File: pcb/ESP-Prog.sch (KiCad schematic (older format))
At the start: 27 parts, among them J1 UJ2-MIBH-G-SMT-TR, J2 Conn_01x03, J3 Conn_02x05_Odd_Even, J4 Conn_01x03, J5 Conn_01x03, J6 Conn_02x03_Odd_Even, Q1 MMSS8050-H-TP, Q2 MMSS8050-H-TP, U1 LD1117S33TR_SOT223

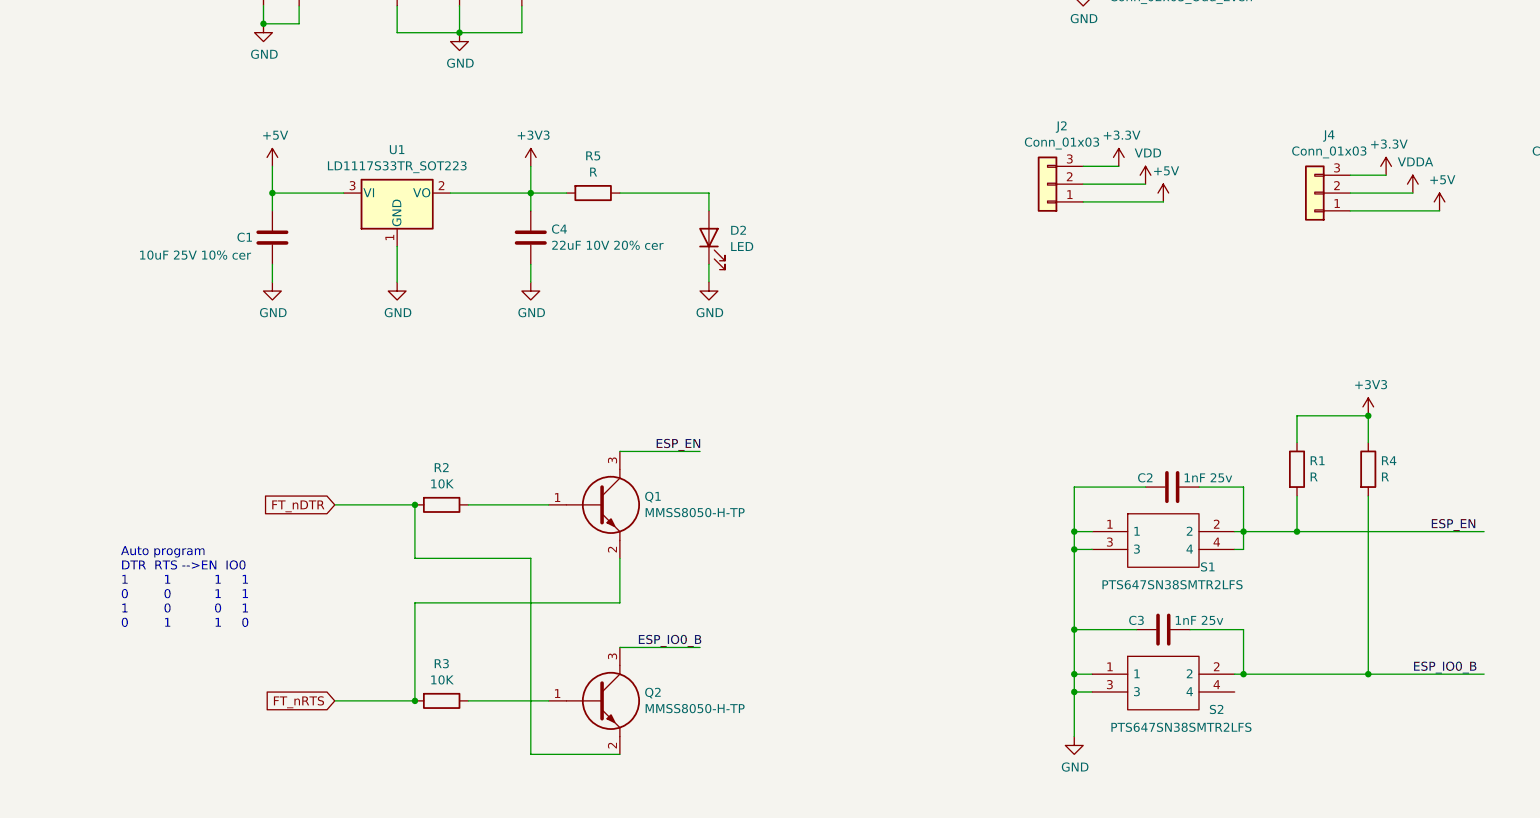
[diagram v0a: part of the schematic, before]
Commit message: correcciones al esquematico y avances en posicionamiento de pcb
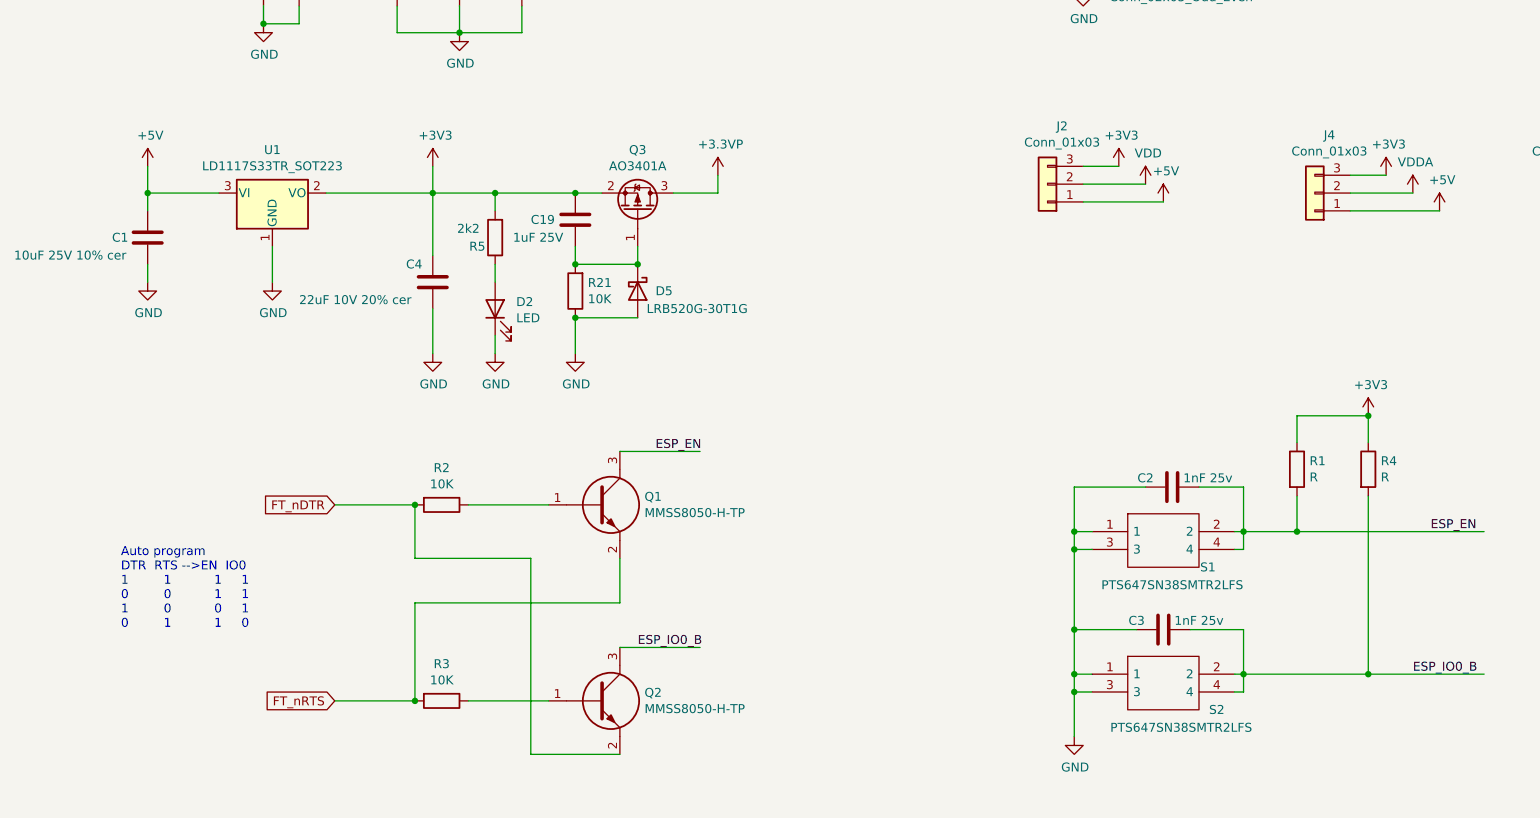
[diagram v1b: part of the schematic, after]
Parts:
- added C19: 1uF 25V, Capacitor_SMD:C_0603_1608Metric, symbol Device:C
- added D5: LRB520G-30T1G, Diode_SMD:D_0603_1608Metric, symbol Device:D_Schottky
- added Q3: AO3401A, Package_TO_SOT_SMD:SOT-23, symbol Transistor_FET:AO3401A
- added R21: 10K, Resistor_SMD:R_0603_1608Metric, symbol Device:R
- R5: value R -> 2k2
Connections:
- net labels added: +3.3VP
- net labels removed: +3.3V
- wire segments 106 -> 117
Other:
- moved on the sheet: C1, C4, D2, R5, U1

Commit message: - Se modifica el esquemático para respetar la estructura gerarquica
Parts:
- removed C1: 10uF 25V 10% cer, Capacitor_SMD:C_0603_1608Metric, symbol Device:C
- removed C19: 1uF 25V, Capacitor_SMD:C_0603_1608Metric, symbol Device:C
- removed C2, C3: 1nF 25v, Capacitor_SMD:C_0603_1608Metric, symbol Device:C
- removed C4: 22uF 10V 20% cer, Capacitor_SMD:C_0603_1608Metric, symbol Device:C
- removed C7, C8: 0.1uF 25v, Capacitor_SMD:C_0603_1608Metric, symbol Device:C
- removed D1: BAT760-7, Diode_SMD:D_SOD-323, symbol SamacSys_Parts:BAT760-7
- removed D2: LED, LED_SMD:LED_0603_1608Metric, symbol Device:LED
- removed D5: LRB520G-30T1G, Diode_SMD:D_0603_1608Metric, symbol Device:D_Schottky
- removed D7, D8, D9: D_TVS, Diode_SMD:D_SOD-523, symbol Device:D_TVS
- removed J1: UJ2-MIBH-G-SMT-TR, SamacSys_Parts:UJ2MIBHGSMTTR, symbol SamacSys_Parts:UJ2-MIBH-G-SMT-TR
- removed J2, J4, J5: Conn_01x03, Connector_PinHeader_2.54mm:PinHeader_1x03_P2.54mm_Vertical, symbol Connector_Generic:Conn_01x03
- removed J3: Conn_02x05_Odd_Even, Connector_PinHeader_1.27mm:PinHeader_2x05_P1.27mm_Vertical_SMD, symbol Connector_Generic:Conn_02x05_Odd_Even
- removed J6: Conn_02x03_Odd_Even, Connector_PinHeader_1.27mm:PinHeader_2x05_P1.27mm_Vertical_SMD, symbol Connector_Generic:Conn_02x03_Odd_Even
- removed Q1, Q2: MMSS8050-H-TP, SamacSys_Parts:SI2305TP, symbol SamacSys_Parts:MMSS8050-H-TP
- removed Q3: AO3401A, Package_TO_SOT_SMD:SOT-23, symbol Transistor_FET:AO3401A
- removed R1, R4: R, Resistor_SMD:R_0603_1608Metric, symbol Device:R
- removed R2, R21, R3: 10K, Resistor_SMD:R_0603_1608Metric, symbol Device:R
- removed R5: 2k2, Resistor_SMD:R_0603_1608Metric, symbol Device:R
- removed S1, S2: PTS647SN38SMTR2LFS, SamacSys_Parts:PTS647SM38SMTR2LFS, symbol SamacSys_Parts:PTS647SN38SMTR2LFS
- removed U1: LD1117S33TR_SOT223, Package_TO_SOT_SMD:SOT-223-3_TabPin2, symbol Regulator_Linear:LD1117S33TR_SOT223
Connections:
- net labels removed: +3.3VP, +3V3, +5V, ESP_EN, ESP_IO0, ESP_IO0_B, ESP_RXD0, ESP_TCK, ESP_TDI, ESP_TDO, ESP_TMS, ESP_TXD0, FT_nDTR, FT_nRTS, GND, USB_DM, USB_DP, VDD, VDDA
- wire segments 117 -> 11
- no-connect marks 3 -> 0
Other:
- note removed: "Auto program\nDTR RTS -->EN IO0\n1 1 1 1\n0 0 1 1\n1 0 0 1\n0 1 1 0"

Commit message: revisiones
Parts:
- added FID1, FID2, FID3: Fiducial, Fiducial:Fiducial_0.5mm_Mask1mm, symbol Mechanical:Fiducial
- added H1: MountingHole, MountingHole:MountingHole_2.5mm, symbol Mechanical:MountingHole
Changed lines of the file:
@@
 Title "Espressif Programmer"
 Date "2021-07-04"
-Rev "1.1"
+Rev "1.2"
 Comp "Sipel SRL"
 Comment1 "Autor: Gonzalo Sanhez"
 Comment2 "Licencia: Open source hardware"
-Comment3 ""
+Comment3 "Programador y debugger para modulos Espressif "
 Comment4 ""
 $EndDescr
@@
 Wire Wire Line
 	4700 3050 5700 3050
+$Comp
+L Mechanical:Fiducial FID2
+U 1 1 61221B37
+P 3250 5250
+F 0 "FID2" H 3335 5296 50  0000 L CNN
+F 1 "Fiducial" H 3335 5205 50  0000 L CNN
+F 2 "Fiducial:Fiducial_0.5mm_Mask1mm" H 3250 5250 50  0001 C CNN
+F 3 "~" H 3250 5250 50  0001 C CNN
+	1    3250 5250
+	1    0    0    -1
+$EndComp
+$Comp
+L Mechanical:Fiducial FID3
+U 1 1 61222291
+P 4100 5250
+F 0 "FID3" H 4185 5296 50  0000 L CNN
+F 1 "Fiducial" H 4185 5205 50  0000 L CNN
+F 2 "Fiducial:Fiducial_0.5mm_Mask1mm" H 4100 5250 50  0001 C CNN
+F 3 "~" H 4100 5250 50  0001 C CNN
+	1    4100 5250
+	1    0    0    -1
+$EndComp
+$Comp
+L Mechanical:Fiducial FID1
+U 1 1 612227C4
+P 2700 5250
+F 0 "FID1" H 2785 5296 50  0000 L CNN
+F 1 "Fiducial" H 2785 5205 50  0000 L CNN
+F 2 "Fiducial:Fiducial_0.5mm_Mask1mm" H 2700 5250 50  0001 C CNN
+F 3 "~" H 2700 5250 50  0001 C CNN
+	1    2700 5250
+	1    0    0    -1
+$EndComp
+$Comp
+L Mechanical:MountingHole H1
+U 1 1 6122523B
+P 4900 5250
+F 0 "H1" H 5000 5296 50  0000 L CNN
+F 1 "MountingHole" H 5000 5205 50  0000 L CNN
+F 2 "MountingHole:MountingHole_2.5mm" H 4900 5250 50  0001 C CNN
+F 3 "~" H 4900 5250 50  0001 C CNN
+	1    4900 5250
+	1    0    0    -1
+$EndComp
 $EndSCHEMATC
